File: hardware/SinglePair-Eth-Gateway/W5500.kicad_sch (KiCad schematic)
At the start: 36 parts, among them U501 7499010211A, U502 W5500, Y501 830108212509

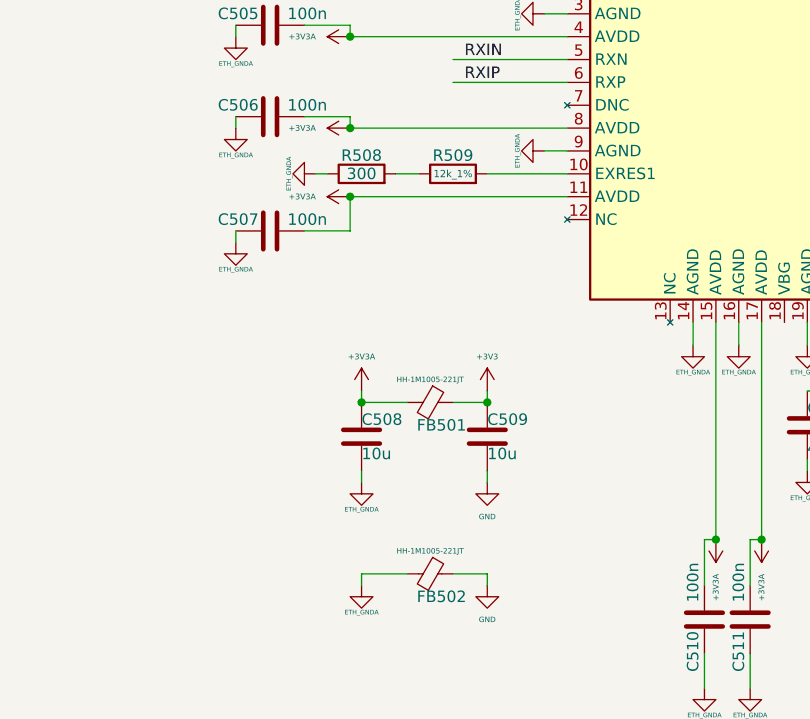
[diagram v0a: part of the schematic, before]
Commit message: Change position of values on the Fab layer
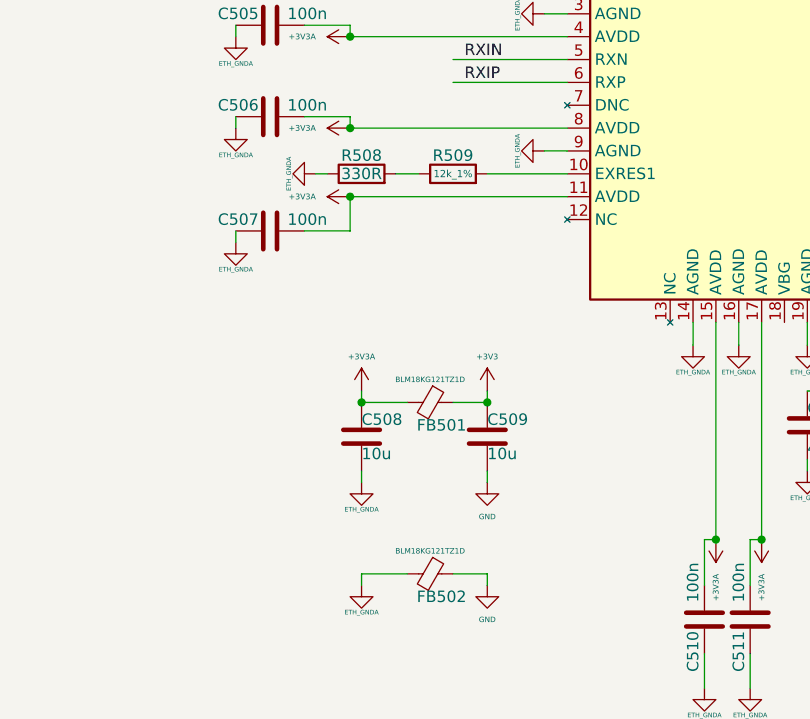
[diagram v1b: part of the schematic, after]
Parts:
- FB501, FB502: value HH-1M1005-221JT -> BLM18KG121TZ1D
- R508: value 300 -> 330R
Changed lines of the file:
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@@
       (effects (font (size 1.27 1.27)))
     )
-    (property "Value" "300" (at 196.85 157.48 90)
+    (property "Value" "330R" (at 196.85 157.48 90)
       (effects (font (size 1.27 1.27)))
     )
@@
       (effects (font (size 1.27 1.27)))
     )
-    (property "Value" "HH-1M1005-221JT" (at 204.47 199.39 90)
+    (property "Value" "BLM18KG121TZ1D" (at 204.47 199.39 90)
       (effects (font (size 0.6 0.6)))
     )
@@
       (effects (font (size 1.27 1.27)))
     )
-    (property "Value" "HH-1M1005-221JT" (at 204.47 180.34 90)
+    (property "Value" "BLM18KG121TZ1D" (at 204.47 180.34 90)
       (effects (font (size 0.6 0.6)))
     )
